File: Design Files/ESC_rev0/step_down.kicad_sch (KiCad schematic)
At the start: 10 parts, among them U4 AMS1117-3.3

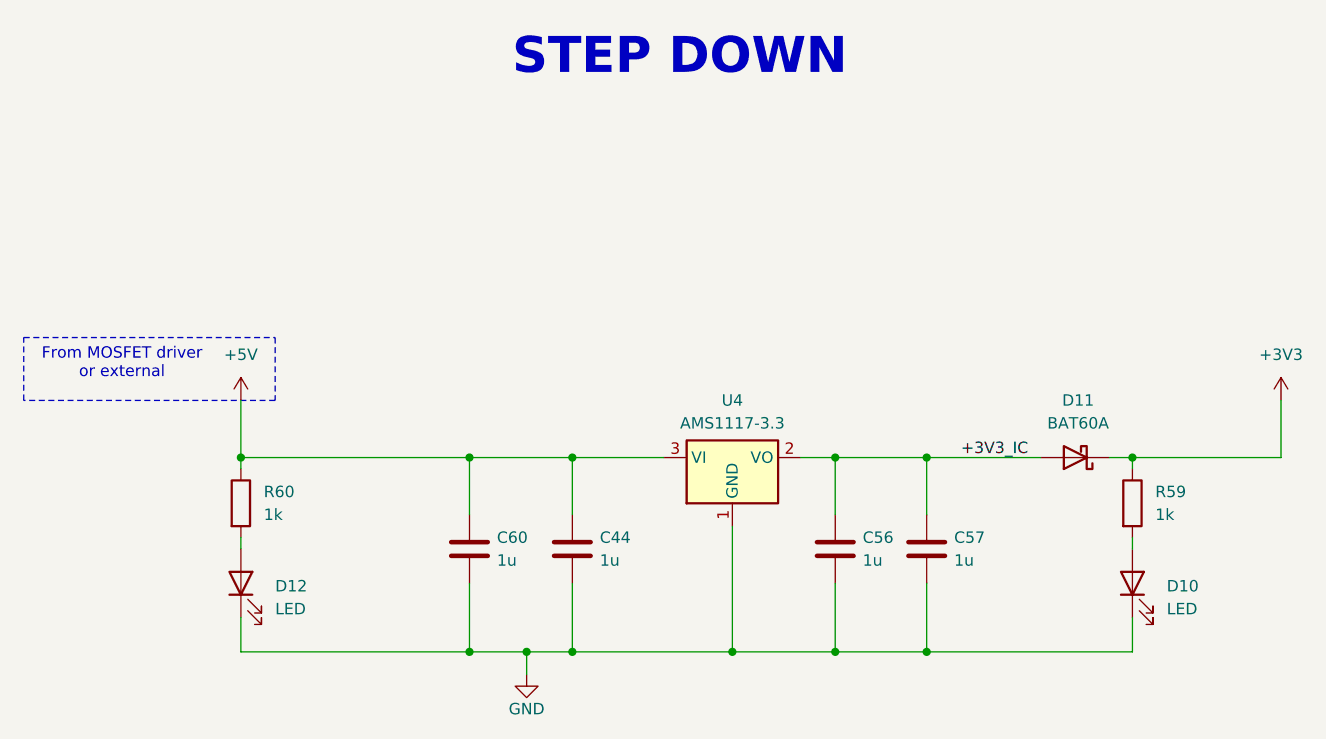
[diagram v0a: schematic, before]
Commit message: UPDATE 12
started schematics revision: edit and added info and circuits to some pages and assigned some footprints for components
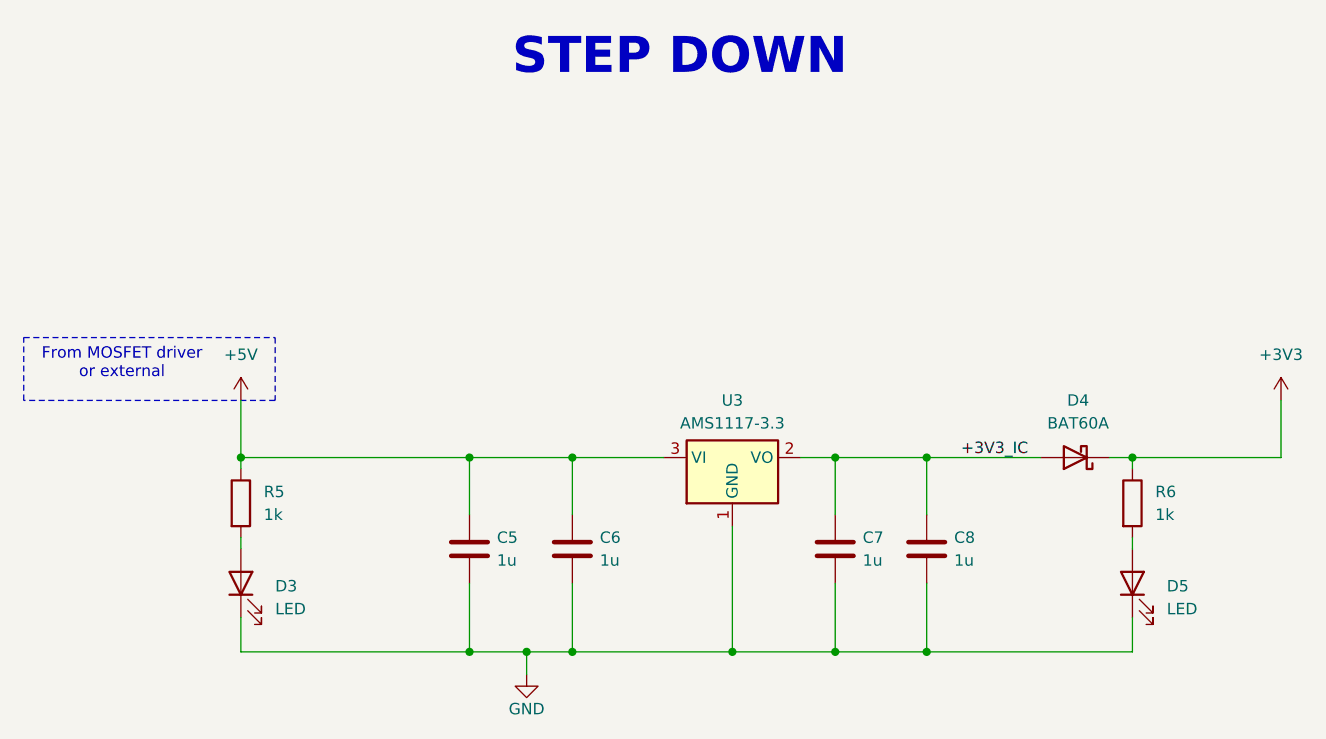
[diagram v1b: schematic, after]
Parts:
- C5: renamed from C60; footprint (none) -> Capacitor_SMD:C_0201_0603Metric
- C6: renamed from C44; footprint (none) -> Capacitor_SMD:C_0201_0603Metric
- C7: renamed from C56; footprint (none) -> Capacitor_SMD:C_0201_0603Metric
- C8: renamed from C57; footprint (none) -> Capacitor_SMD:C_0201_0603Metric
- D3: renamed from D12; footprint (none) -> LED_SMD:LED_0201_0603Metric
- D5: renamed from D10; footprint (none) -> LED_SMD:LED_0201_0603Metric
- renumbered D11 to D4, R60 to R5, R59 to R6, U4 to U3
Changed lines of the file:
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@@
 		(on_board yes)
 		(dnp no)
-		(property "Reference" "C44"
+		(property "Reference" "C6"
 			(at 138.938 93.98 0)
 			(effects
@@
 			)
 		)
-		(property "Footprint" ""
+		(property "Footprint" "Capacitor_SMD:C_0201_0603Metric"
 			(at 136.8552 99.06 0)
 			(effects
@@
 			(project "ESC_rev0"
 				(path "/7906e740-34c4-4b06-b70f-1daa08872946/283d0162-bde7-4442-bcf2-ede56253b6d8"
-					(reference "C44")
+					(reference "C6")
 					(unit 1)
 				)
@@
 		(dnp no)
 		(fields_autoplaced yes)
-		(property "Reference" "D10"
+		(property "Reference" "D5"
 			(at 201.93 99.3774 90)
 			(effects
@@
 			)
 		)
-		(property "Footprint" ""
+		(property "Footprint" "LED_SMD:LED_0201_0603Metric"
 			(at 198.12 99.06 0)
 			(effects
@@
 			(project "ESC_rev0"
 				(path "/7906e740-34c4-4b06-b70f-1daa08872946/283d0162-bde7-4442-bcf2-ede56253b6d8"
-					(reference "D10")
+					(reference "D5")
 					(unit 1)
 				)
@@
 		(dnp no)
 		(fields_autoplaced yes)
-		(property "Reference" "U4"
+		(property "Reference" "U3"
 			(at 153.67 78.74 0)
 			(effects
@@
 		(pin "3"
 		)
+		(instances
+			(project ""
+				(path "/7906e740-34c4-4b06-b70f-1daa08872946/283d0162-bde7-4442-bcf2-ede56253b6d8"
+					(reference "U3")
+					(unit 1)
+				)
+			)
+		)
 	)
 	(symbol
@@
 		(dnp no)
 		(fields_autoplaced yes)
-		(property "Reference" "R60"
+		(property "Reference" "R5"
 			(at 101.6 88.8999 0)
 			(effects
@@
 		(pin "1"
 		)
+		(instances
+			(project ""
+				(path "/7906e740-34c4-4b06-b70f-1daa08872946/283d0162-bde7-4442-bcf2-ede56253b6d8"
+					(reference "R5")
+					(unit 1)
+				)
+			)
+		)
 	)
 	(symbol
@@
 		(dnp no)
 		(fields_autoplaced yes)
-		(property "Reference" "D11"
+		(property "Reference" "D4"
 			(at 192.0875 78.74 0)
 			(effects
@@
 		(pin "1"
 		)
+		(instances
+			(project ""
+				(path "/7906e740-34c4-4b06-b70f-1daa08872946/283d0162-bde7-4442-bcf2-ede56253b6d8"
+					(reference "D4")
+					(unit 1)
+				)
+			)
+		)
 	)
 	(symbol
@@
 		(on_board yes)
 		(dnp no)
-		(property "Reference" "C60"
+		(property "Reference" "C5"
 			(at 127.508 93.98 0)
 			(effects
@@
 			)
 		)
-		(property "Footprint" ""
+		(property "Footprint" "Capacitor_SMD:C_0201_0603Metric"
 			(at 125.4252 99.06 0)
 			(effects
@@
 		(pin "2"
 		)
+		(instances
+			(project ""
+				(path "/7906e740-34c4-4b06-b70f-1daa08872946/283d0162-bde7-4442-bcf2-ede56253b6d8"
+					(reference "C5")
+					(unit 1)
+				)
+			)
+		)
 	)
 	(symbol
@@
 		(on_board yes)
 		(dnp no)
-		(property "Reference" "#PWR083"
+		(property "Reference" "#PWR010"
 			(at 130.81 115.57 0)
 			(effects
@@
 			(project "ESC_rev0"
 				(path "/7906e740-34c4-4b06-b70f-1daa08872946/283d0162-bde7-4442-bcf2-ede56253b6d8"
-					(reference "#PWR083")
+					(reference "#PWR010")
 					(unit 1)
 				)
@@
 		(on_board yes)
 		(dnp no)
-		(property "Reference" "C56"
+		(property "Reference" "C7"
 			(at 168.148 93.98 0)
 			(effects
@@
 			)
 		)
-		(property "Footprint" ""
+		(property "Footprint" "Capacitor_SMD:C_0201_0603Metric"
 			(at 166.0652 99.06 0)
 			(effects
@@
 			(project "ESC_rev0"
 				(path "/7906e740-34c4-4b06-b70f-1daa08872946/283d0162-bde7-4442-bcf2-ede56253b6d8"
-					(reference "C56")
+					(reference "C7")
 					(unit 1)
 				)
@@
 		(dnp no)
 		(fields_autoplaced yes)
-		(property "Reference" "#PWR085"
+		(property "Reference" "#PWR09"
 			(at 99.06 82.55 0)
 			(effects
@@
 		(pin "1"
 		)
+		(instances
+			(project ""
+				(path "/7906e740-34c4-4b06-b70f-1daa08872946/283d0162-bde7-4442-bcf2-ede56253b6d8"
+					(reference "#PWR09")
+					(unit 1)
+				)
+			)
+		)
 	)
 	(symbol
@@
 		(dnp no)
 		(fields_autoplaced yes)
-		(property "Reference" "D12"
+		(property "Reference" "D3"
 			(at 102.87 99.3774 90)
 			(effects
@@
 			)
 		)
-		(property "Footprint" ""
+		(property "Footprint" "LED_SMD:LED_0201_0603Metric"
 			(at 99.06 99.06 0)
 			(effects
@@
 		(pin "1"
 		)
+		(instances
+			(project ""
+				(path "/7906e740-34c4-4b06-b70f-1daa08872946/283d0162-bde7-4442-bcf2-ede56253b6d8"
+					(reference "D3")
+					(unit 1)
+				)
+			)
+		)
 	)
 	(symbol
@@
 		(dnp no)
 		(fields_autoplaced yes)
-		(property "Reference" "R59"
+		(property "Reference" "R6"
 			(at 200.66 88.8999 0)
 			(effects
@@
 			(project "ESC_rev0"
 				(path "/7906e740-34c4-4b06-b70f-1daa08872946/283d0162-bde7-4442-bcf2-ede56253b6d8"
-					(reference "R59")
+					(reference "R6")
 					(unit 1)
 				)
@@
 		(on_board yes)
 		(dnp no)
-		(property "Reference" "C57"
+		(property "Reference" "C8"
 			(at 178.308 93.98 0)
 			(effects
@@
 			)
 		)
-		(property "Footprint" ""
+		(property "Footprint" "Capacitor_SMD:C_0201_0603Metric"
 			(at 176.2252 99.06 0)
 			(effects
@@
 			(project "ESC_rev0"
 				(path "/7906e740-34c4-4b06-b70f-1daa08872946/283d0162-bde7-4442-bcf2-ede56253b6d8"
-					(reference "C57")
+					(reference "C8")
 					(unit 1)
 				)
@@
 		(dnp no)
 		(fields_autoplaced yes)
-		(property "Reference" "#PWR087"
+		(property "Reference" "#PWR011"
 			(at 214.63 82.55 0)
 			(effects
@@
 		(pin "1"
 		)
-	)
+		(instances
+			(project ""
+				(path "/7906e740-34c4-4b06-b70f-1daa08872946/283d0162-bde7-4442-bcf2-ede56253b6d8"
+					(reference "#PWR011")
+					(unit 1)
+				)
+			)
+		)
+	)

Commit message: update 13
assigned all footprints (provisionally) and imported them - errors and warning occurred, must be corrected in the future
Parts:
- R5, R6: footprint (none) -> Resistor_SMD:R_0603_1608Metric
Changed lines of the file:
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@@
 			)
 		)
-		(property "Footprint" ""
+		(property "Footprint" "Resistor_SMD:R_0603_1608Metric"
 			(at 97.282 90.17 90)
 			(effects
@@
 			)
 		)
-		(property "Footprint" ""
+		(property "Footprint" "Resistor_SMD:R_0603_1608Metric"
 			(at 196.342 90.17 90)
 			(effects

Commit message: update 16
All components placed on board. Some components modifications and addition were made: added 3D models, changed some symbols and footprints positions and some component types.
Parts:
- C5, C6, C7, C8: footprint Capacitor_SMD:C_0201_0603Metric -> Capacitor_SMD:C_0603_1608Metric
- D3, D5: footprint LED_SMD:LED_0201_0603Metric -> LED_SMD:LED_0805_2012Metric
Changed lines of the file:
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@@
 			)
 		)
-		(property "Footprint" "Capacitor_SMD:C_0201_0603Metric"
+		(property "Footprint" "Capacitor_SMD:C_0603_1608Metric"
 			(at 136.8552 99.06 0)
 			(effects
@@
 			)
 		)
-		(property "Footprint" "LED_SMD:LED_0201_0603Metric"
+		(property "Footprint" "LED_SMD:LED_0805_2012Metric"
 			(at 198.12 99.06 0)
 			(effects
@@
 			)
 		)
-		(property "Footprint" "Capacitor_SMD:C_0201_0603Metric"
+		(property "Footprint" "Capacitor_SMD:C_0603_1608Metric"
 			(at 125.4252 99.06 0)
 			(effects
@@
 			)
 		)
-		(property "Footprint" "Capacitor_SMD:C_0201_0603Metric"
+		(property "Footprint" "Capacitor_SMD:C_0603_1608Metric"
 			(at 166.0652 99.06 0)
 			(effects
@@
 			)
 		)
-		(property "Footprint" "LED_SMD:LED_0201_0603Metric"
+		(property "Footprint" "LED_SMD:LED_0805_2012Metric"
 			(at 99.06 99.06 0)
 			(effects
@@
 			)
 		)
-		(property "Footprint" "Capacitor_SMD:C_0201_0603Metric"
+		(property "Footprint" "Capacitor_SMD:C_0603_1608Metric"
 			(at 176.2252 99.06 0)
 			(effects
